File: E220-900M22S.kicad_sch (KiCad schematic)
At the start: 1 part, among them U2 RFM95W-915S2

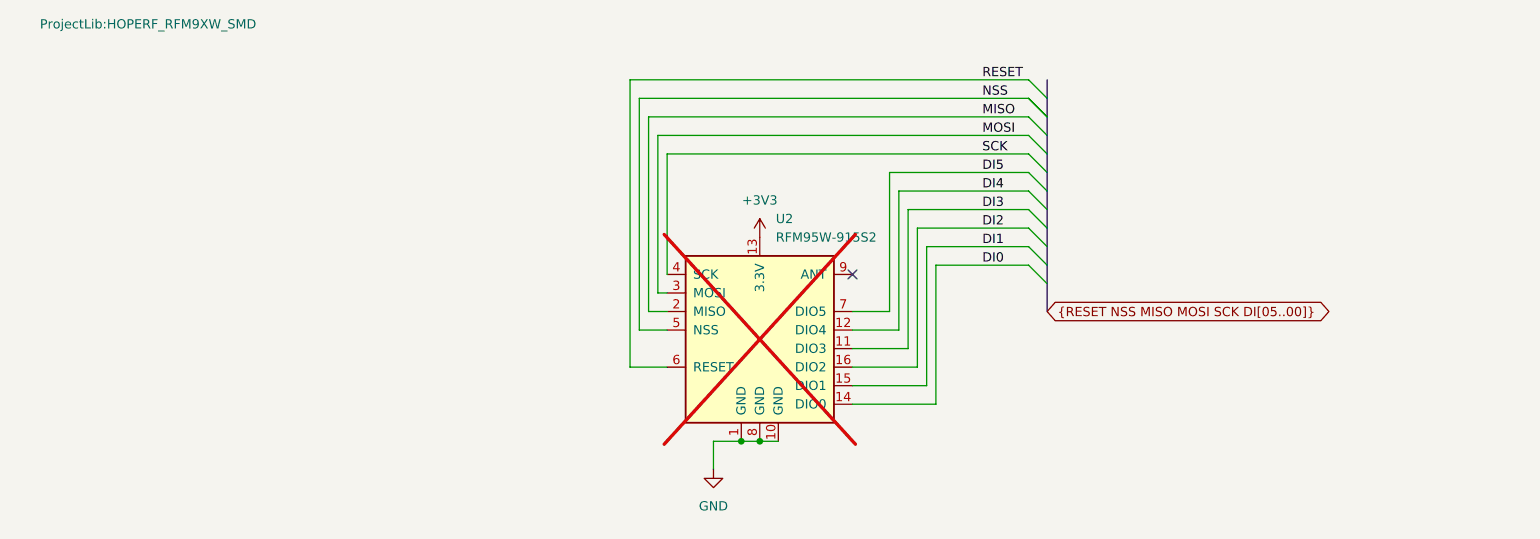
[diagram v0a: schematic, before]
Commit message: e220 schematic needs work, and proper DIO connections. Switching back to radio-sx127.
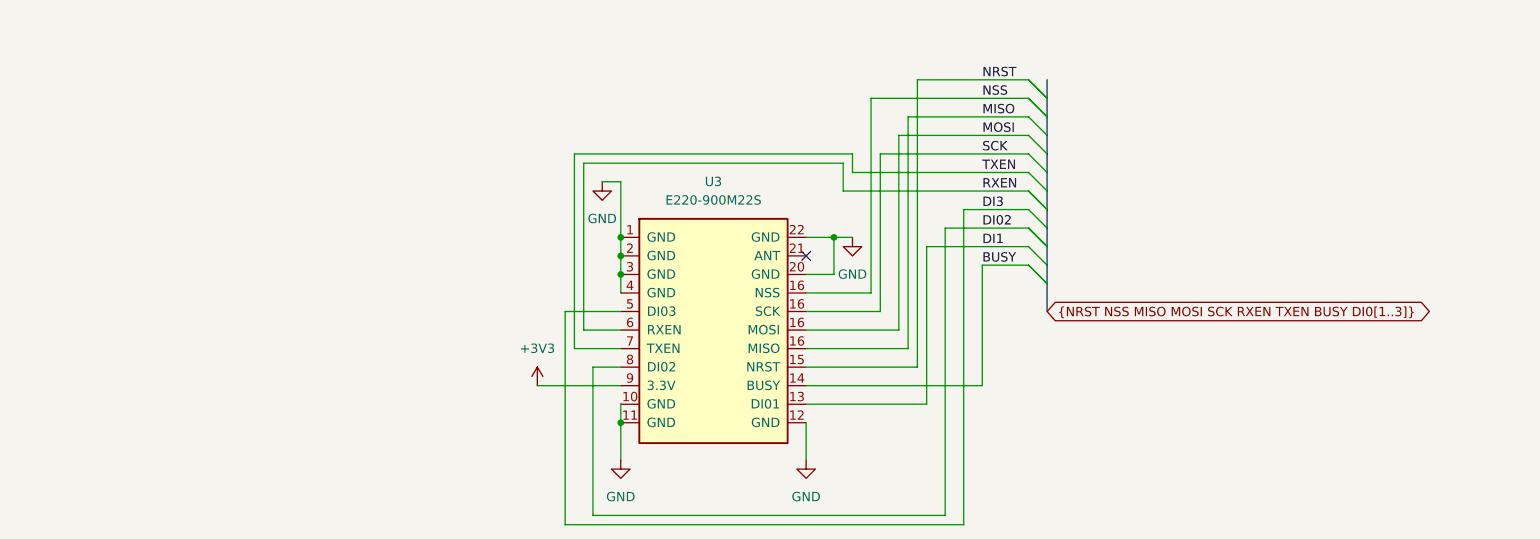
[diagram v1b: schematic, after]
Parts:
- removed U2: RFM95W-915S2, ProjectLib:HOPERF_RFM9XW_SMD, symbol ProjectLib:RFM95W-915S2
- added U3: E220-900M22S, symbol ProjectLib:E220-900M22S
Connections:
- net +3V3: now also U3.9 (3.3V)
- net DI1: now also U3.13 (DI01)
- net DI3: now also U3.5 (DI03)
- net GND: now also U3.1 (GND), U3.10 (GND), U3.11 (GND), U3.12 (GND), U3.2 (GND), U3.20 (GND), U3.22 (GND), U3.3 (GND), U3.4 (GND)
- net MISO: now also U3.16 (SCK)
- net MOSI: now also U3.16 (SCK)
- net NSS: now also U3.16 (SCK)
- net SCK: now also U3.16 (SCK)
- new net BUSY: U3.14 (BUSY)
- new net DI02: U3.8 (DI02)
- new net NRST: U3.15 (NRST)
- new net RXEN: U3.6 (RXEN)
- new net TXEN: U3.7 (TXEN)

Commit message: some cleanup. About to split two lra module branches.
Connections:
- net DI1 renamed DI01
- net DI3 renamed DI03
